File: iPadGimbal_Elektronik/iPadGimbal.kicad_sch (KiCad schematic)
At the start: 12 parts, among them J1 Conn_01x05, J2 Conn_01x05, J3 Conn_01x02, J4 Conn_01x02, J5 Conn_01x02, U1 ESP32-DEVKITC-32D, U2 ULN2003A, U3 ULN2003A

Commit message: Silkscreen angepasst
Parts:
- J1, J2: footprint Connector_JST:JST_EH_B5B-EH-A_1x05_P2.50mm_Vertical -> Connector_JST:JST_XH_B5B-XH-AM_1x05_P2.50mm_Vertical
- J3, J4: footprint Connector_JST:JST_EH_B2B-EH-A_1x02_P2.50mm_Vertical -> Connector_JST:JST_XH_B2B-XH-AM_1x02_P2.50mm_Vertical
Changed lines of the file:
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@@
       (effects (font (size 1.27 1.27)) (justify left))
     )
-    (property "Footprint" "Connector_JST:JST_EH_B2B-EH-A_1x02_P2.50mm_Vertical" (id 2) (at 116.84 146.05 0)
+    (property "Footprint" "Connector_JST:JST_XH_B2B-XH-AM_1x02_P2.50mm_Vertical" (id 2) (at 116.84 146.05 0)
       (effects (font (size 1.27 1.27)) hide)
     )
@@
       (effects (font (size 1.27 1.27)) (justify left))
     )
-    (property "Footprint" "Connector_JST:JST_EH_B5B-EH-A_1x05_P2.50mm_Vertical" (id 2) (at 219.71 50.8 0)
+    (property "Footprint" "Connector_JST:JST_XH_B5B-XH-AM_1x05_P2.50mm_Vertical" (id 2) (at 219.71 50.8 0)
       (effects (font (size 1.27 1.27)) hide)
     )
@@
       (effects (font (size 1.27 1.27)) (justify left))
     )
-    (property "Footprint" "Connector_JST:JST_EH_B5B-EH-A_1x05_P2.50mm_Vertical" (id 2) (at 220.98 101.6 0)
+    (property "Footprint" "Connector_JST:JST_XH_B5B-XH-AM_1x05_P2.50mm_Vertical" (id 2) (at 220.98 101.6 0)
       (effects (font (size 1.27 1.27)) hide)
     )
@@
       (effects (font (size 1.27 1.27)) (justify left))
     )
-    (property "Footprint" "Connector_JST:JST_EH_B2B-EH-A_1x02_P2.50mm_Vertical" (id 2) (at 116.84 160.02 0)
+    (property "Footprint" "Connector_JST:JST_XH_B2B-XH-AM_1x02_P2.50mm_Vertical" (id 2) (at 116.84 160.02 0)
       (effects (font (size 1.27 1.27)) hide)
     )
@@
     )
     (path "/28f575a2-f706-4636-b663-e8d0eeffb6dd"
-      (reference "J1") (unit 1) (value "Conn_01x05") (footprint "Connector_JST:JST_EH_B5B-EH-A_1x05_P2.50mm_Vertical")
+      (reference "J1") (unit 1) (value "Conn_01x05") (footprint "Connector_JST:JST_XH_B5B-XH-AM_1x05_P2.50mm_Vertical")
     )
     (path "/53a9d5d0-96ca-4248-a1bc-e298ff09b21e"
-      (reference "J2") (unit 1) (value "Conn_01x05") (footprint "Connector_JST:JST_EH_B5B-EH-A_1x05_P2.50mm_Vertical")
+      (reference "J2") (unit 1) (value "Conn_01x05") (footprint "Connector_JST:JST_XH_B5B-XH-AM_1x05_P2.50mm_Vertical")
     )
     (path "/1a41eef7-d22d-4c98-bc36-4c3c8c34efa4"
-      (reference "J3") (unit 1) (value "Conn_01x02") (footprint "Connector_JST:JST_EH_B2B-EH-A_1x02_P2.50mm_Vertical")
+      (reference "J3") (unit 1) (value "Conn_01x02") (footprint "Connector_JST:JST_XH_B2B-XH-AM_1x02_P2.50mm_Vertical")
     )
     (path "/70df5d0f-d740-4377-affe-b0b200467c6f"
-      (reference "J4") (unit 1) (value "Conn_01x02") (footprint "Connector_JST:JST_EH_B2B-EH-A_1x02_P2.50mm_Vertical")
+      (reference "J4") (unit 1) (value "Conn_01x02") (footprint "Connector_JST:JST_XH_B2B-XH-AM_1x02_P2.50mm_Vertical")
     )
     (path "/199067cf-8430-4111-a32d-cb590ddc2988"

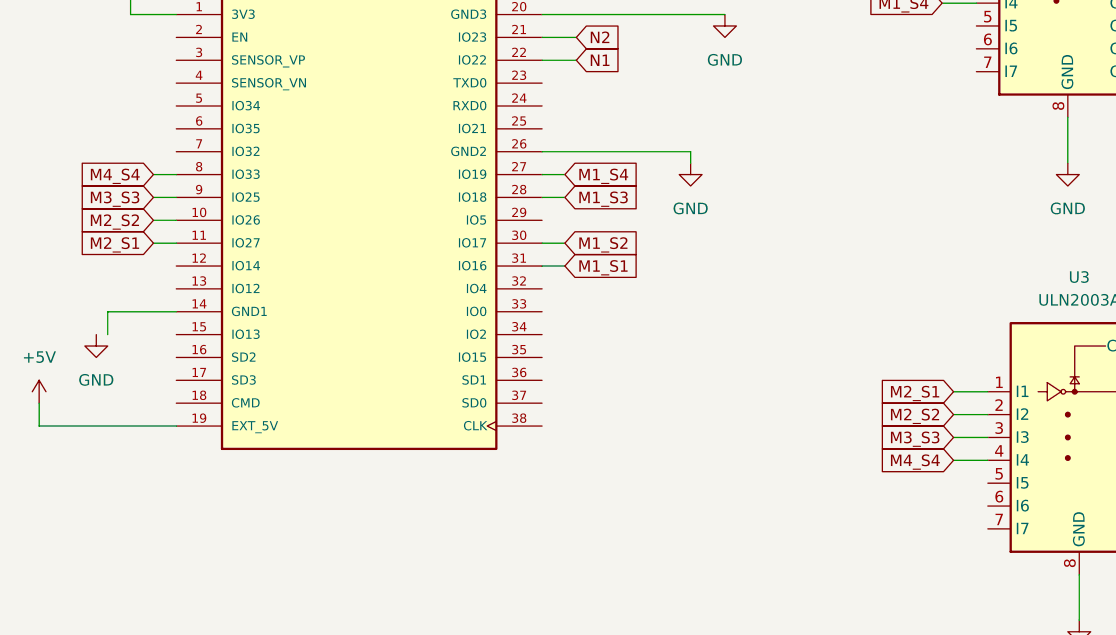
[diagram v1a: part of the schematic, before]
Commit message: Bennenung im Schaltplan korregiert; MassePin des ESP's korregiert
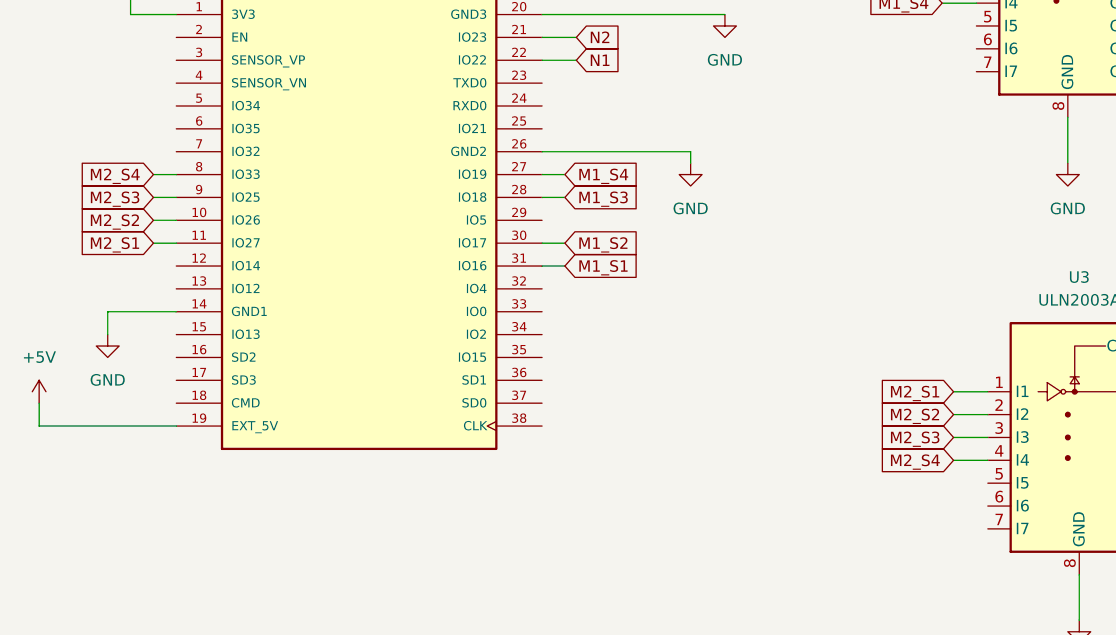
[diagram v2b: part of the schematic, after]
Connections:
- net GND: now also U1.14 (GND1)
- net M3_S3 renamed M2_S3
- net M4_S4 renamed M2_S4
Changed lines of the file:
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@@
     )
   )
-  (global_label "M4_S4" (shape input) (at 167.64 106.68 180) (fields_autoplaced)
-    (effects (font (size 1.27 1.27)) (justify right))
-    (property "Intersheet References" "${INTERSHEET_REFS}" (id 0) (at 159.1793 106.7594 0)
-      (effects (font (size 1.27 1.27)) (justify right) hide)
-    )
-  )
-  (global_label "M4_S4" (shape input) (at 78.74 74.93 180) (fields_autoplaced)
-    (effects (font (size 1.27 1.27)) (justify right))
-    (property "Intersheet References" "${INTERSHEET_REFS}" (id 0) (at 70.2793 75.0094 0)
+  (global_label "M2_S4" (shape input) (at 167.64 106.68 180) (fields_autoplaced)
+    (effects (font (size 1.27 1.27)) (justify right))
+    (property "Intersheet References" "${INTERSHEET_REFS}" (id 0) (at 159.1793 106.6006 0)
+      (effects (font (size 1.27 1.27)) (justify right) hide)
+    )
+  )
+  (global_label "M2_S4" (shape input) (at 78.74 74.93 180) (fields_autoplaced)
+    (effects (font (size 1.27 1.27)) (justify right))
+    (property "Intersheet References" "${INTERSHEET_REFS}" (id 0) (at 70.2793 74.8506 0)
       (effects (font (size 1.27 1.27)) (justify right) hide)
     )
@@
     )
   )
-  (global_label "M3_S3" (shape input) (at 167.64 104.14 180) (fields_autoplaced)
-    (effects (font (size 1.27 1.27)) (justify right))
-    (property "Intersheet References" "${INTERSHEET_REFS}" (id 0) (at 159.1793 104.2194 0)
+  (global_label "M2_S3" (shape input) (at 167.64 104.14 180) (fields_autoplaced)
+    (effects (font (size 1.27 1.27)) (justify right))
+    (property "Intersheet References" "${INTERSHEET_REFS}" (id 0) (at 159.1793 104.0606 0)
       (effects (font (size 1.27 1.27)) (justify right) hide)
     )
@@
     )
   )
-  (global_label "M3_S3" (shape input) (at 78.74 77.47 180) (fields_autoplaced)
-    (effects (font (size 1.27 1.27)) (justify right))
-    (property "Intersheet References" "${INTERSHEET_REFS}" (id 0) (at 70.2793 77.5494 0)
+  (global_label "M2_S3" (shape input) (at 78.74 77.47 180) (fields_autoplaced)
+    (effects (font (size 1.27 1.27)) (justify right))
+    (property "Intersheet References" "${INTERSHEET_REFS}" (id 0) (at 70.2793 77.3906 0)
       (effects (font (size 1.27 1.27)) (justify right) hide)
     )
@@
     (pin "1")
   )
-  (symbol (lib_id "power:GND") (at 72.39 92.71 0) (unit 1)
-    (in_bom yes) (on_board yes) (fields_autoplaced)
-    (property "Reference" "#PWR02" (id 0) (at 72.39 99.06 0)
-      (effects (font (size 1.27 1.27)) hide)
-    )
-    (property "Value" "GND" (id 1) (at 72.39 97.79 0))
-    (property "Footprint" "" (id 2) (at 72.39 92.71 0)
-      (effects (font (size 1.27 1.27)) hide)
-    )
-    (property "Datasheet" "" (id 3) (at 72.39 92.71 0)
-      (effects (font (size 1.27 1.27)) hide)
-    )
+  (symbol (lib_id "power:GND") (at 73.66 92.71 0) (unit 1)
+    (in_bom yes) (on_board yes) (fields_autoplaced)
+    (property "Reference" "#PWR02" (id 0) (at 73.66 99.06 0)
+      (effects (font (size 1.27 1.27)) hide)
+    )
+    (property "Value" "GND" (id 1) (at 73.66 97.79 0))
+    (property "Footprint" "" (id 2) (at 73.66 92.71 0)
+      (effects (font (size 1.27 1.27)) hide)
+    )
+    (property "Datasheet" "" (id 3) (at 73.66 92.71 0)
+      (effects (font (size 1.27 1.27)) hide)
+    )
